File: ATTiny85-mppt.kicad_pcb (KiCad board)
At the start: 2 copper layers, 97.6 x 90.8 mm, 56 parts, among them Q1 BUK9511-55A127, Q2 BUK9511-55A127, Q3 2N2222A, Q4 2N2222A, Q5 2N2904A, U1 LM7805_TO220, U2 LM358N, U3 ATtiny85-20PU

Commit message: refine pcb layout.
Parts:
- moved C6 3.78 mm to (65.7, 66.7), turned to 180 degrees
- moved C3 3.76 mm to (75.8, 44.7), turned to 270 degrees
- moved C5 3.23 mm to (79.6, 66.7), turned to 180 degrees
- moved R9 0.34 mm to (112.5, 54.3)
- moved U3 0.31 mm to (90.4, 49.2)
- moved R12 0.24 mm to (53.0, 56.8)
- moved R16 0.22 mm to (84.9, 56.8)
- moved R8 0.15 mm to (58.2, 56.7)
- moved R15 0.13 mm to (71.5, 76.9)
- moved R10 0.10 mm to (108.1, 54.3)
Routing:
- net GND: track 273.6 -> 300.6 mm
- net /BootStrap: track 73.5 -> 82.2 mm
- net /PV-Current: track 42.6 -> 36.5 mm
- net Net-(Q3-Pad3): track 39.8 -> 34.1 mm
- net Net-(C2-Pad1): track 36.8 -> 32.8 mm
- net Net-(R6-Pad2): track 48.9 -> 52.6 mm
- net /3.6v: track 117.9 -> 114.2 mm
- net Net-(R1-Pad2): track 27.3 -> 28.9 mm
- net Net-(C6-Pad1): track 31.8 -> 33.4 mm
- net Net-(R11-Pad1): track 33.9 -> 35.0 mm

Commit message: rearrange.
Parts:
- C2: value 47uF 50v -> 22uF 50v
- D12: value BZX 55c12(12V) -> Optinal Zenner
- D3: value 1N4001 -> 1N4148
- Q5: value 2N2904A -> 2N2907A
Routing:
- net GND: track 300.6 -> 306.2 mm
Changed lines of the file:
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@@
     (thickness 1.6)
     (drawings 7)
-    (tracks 301)
+    (tracks 303)
     (zones 0)
     (modules 56)
@@
   )
   (setup
-    (last_trace_width 1.5)
+    (last_trace_width 0.25)
     (user_trace_width 0.5)
     (user_trace_width 1)
@@
       (effects (font (size 1 1) (thickness 0.15)))
     )
-    (fp_text value 1N4001 (at 5.08 2.41 180) (layer F.Fab)
+    (fp_text value 1N4148 (at 5.08 2.41 180) (layer F.Fab)
       (effects (font (size 1 1) (thickness 0.15)))
     )
@@
       (effects (font (size 1 1) (thickness 0.15)))
     )
-    (fp_text value "47uF 50v" (at 2.5 7.56) (layer F.Fab)
+    (fp_text value "22uF 50v" (at 2.5 7.56) (layer F.Fab)
       (effects (font (size 1 1) (thickness 0.15)))
     )
@@
       (effects (font (size 1 1) (thickness 0.15)))
     )
-    (fp_text value 2N2904A (at 2.32156 -4.00304 90) (layer F.Fab)
+    (fp_text value 2N2907A (at 2.32156 -4.00304 90) (layer F.Fab)
       (effects (font (size 1 1) (thickness 0.15)))
     )
@@
       (effects (font (size 1 1) (thickness 0.15)))
     )
-    (fp_text value "BZX 55c12(12V)" (at 5.08 2.41) (layer F.Fab)
+    (fp_text value "Optinal Zenner" (at 5.08 2.41) (layer F.Fab)
       (effects (font (size 1 1) (thickness 0.15)))
     )
@@
   (segment (start 75.83932 65.46976) (end 74.58328 66.7258) (width 2) (layer B.Cu) (net 6))
   (segment (start 75.83932 49.7294) (end 75.83932 65.46976) (width 2) (layer B.Cu) (net 6))
+  (segment (start 93.2184 82.1186) (end 90.297 79.1972) (width 1.2) (layer B.Cu) (net 6))
+  (segment (start 93.2184 83.56216) (end 93.2184 82.1186) (width 1.2) (layer B.Cu) (net 6))
   (segment (start 89.22151 54.32552) (end 89.21135 54.33568) (width 1.2) (layer F.Cu) (net 7))
   (segment (start 90.35288 54.32552) (end 89.22151 54.32552) (width 1.2) (layer F.Cu) (net 7))

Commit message: rearrange lines.
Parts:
- D12: footprint Diodes_THT:D_DO-41_SOD81_P10.16mm_Horizontal -> Diodes_THT:D_DO-41_SOD81_P5.08mm_Vertical_AnodeUp
- moved D12 7.39 mm to (119.0, 31.5)
- moved Q2 3.15 mm to (111.6, 29.4)
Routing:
- net PRI_LO: track 94.1 -> 137.1 mm
- net Net-(C7-Pad1): track 84.3 -> 114.6 mm
- net Net-(D1-Pad1): track 85.1 -> 111.5 mm
- net GND: track 306.2 -> 330.0 mm
- net Net-(C2-Pad2): track 50.8 -> 60.0 mm
- net Net-(D12-Pad1): track 11.7 -> 19.2 mm
- net +24V: track 29.3 -> 33.9 mm

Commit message: update
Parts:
- R11: value 100k -> 4.7k
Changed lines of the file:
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@@
   )
   (setup
-    (last_trace_width 1.5)
+    (last_trace_width 0.25)
     (user_trace_width 0.5)
     (user_trace_width 1)
@@
       (effects (font (size 1 1) (thickness 0.15)))
     )
-    (fp_text value 100k (at 7.07644 -2.13868 90) (layer F.Fab)
-      (effects (font (size 1 1) (thickness 0.15)))
-    )
+    (fp_text value 4.7k (at 7.07644 -2.13868 90) (layer F.Fab)
+      (effects (font (size 1 1) (thickness 0.15)))
+    )

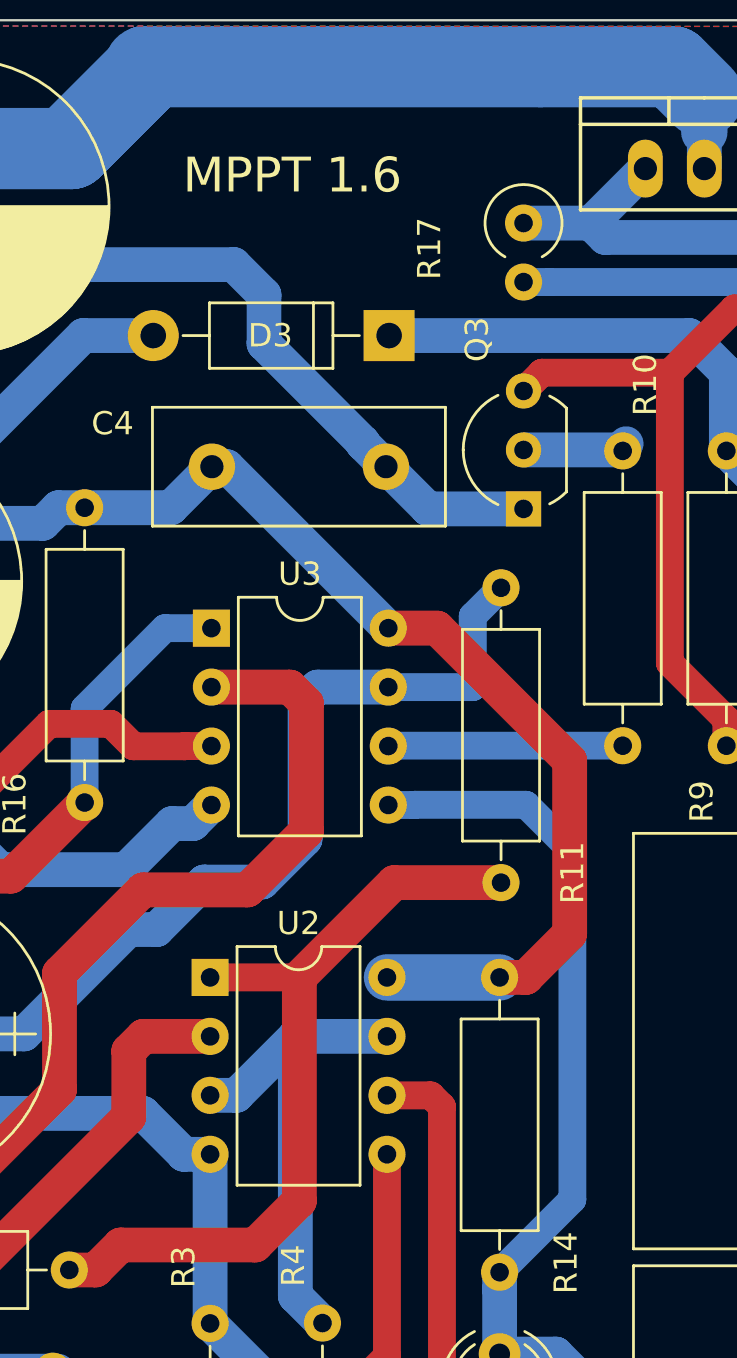
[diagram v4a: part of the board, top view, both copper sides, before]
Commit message: Remove R11 on PCB layout.
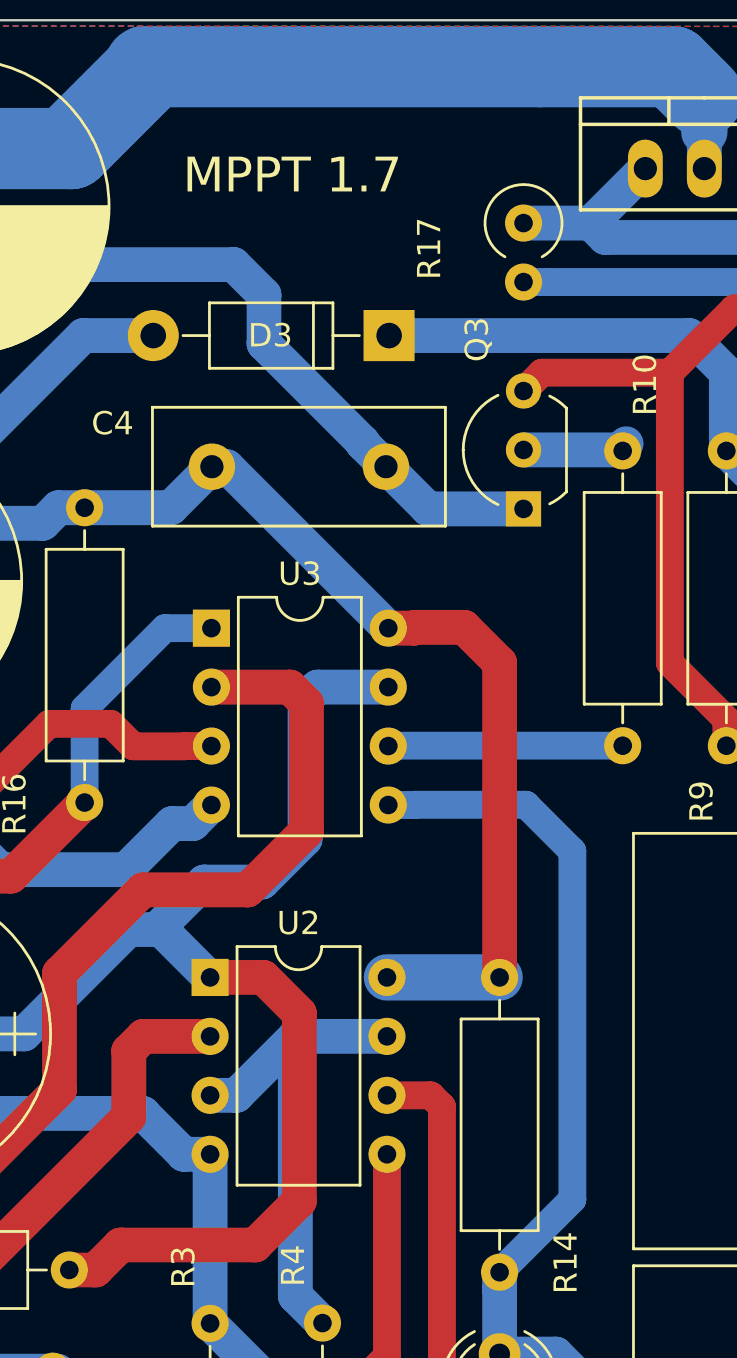
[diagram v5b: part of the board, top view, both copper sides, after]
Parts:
- removed R11: 4.7k, Resistors_THT:R_Axial_DIN0309_L9.0mm_D3.2mm_P12.70mm_Horizontal
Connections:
- R15 pad 2: Net-(R11-Pad1) -> /PV-Current
- U2 pad 1: Net-(R11-Pad1) -> /PV-Current
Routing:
- net Net-(R11-Pad1): track 35.0 -> 0.00 mm
- net /PV-Current: track 36.5 -> 54.9 mm
- net /BootStrap: track 82.2 -> 79.8 mm
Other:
- board text added: "MPPT 1.7"
- board text removed: "MPPT 1.6"

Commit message: update PCB.
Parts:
- removed R17: 1k, Resistors_THT:R_Axial_DIN0309_L9.0mm_D3.2mm_P2.54mm_Vertical
- moved D9 1.18 mm to (103.7, 89.5)
- moved D8 1.09 mm to (103.7, 83.6)
- moved R14 0.92 mm to (103.7, 64.3)
- moved R10 0.16 mm to (107.9, 54.3)
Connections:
- Q4 pad 1: Net-(Q4-Pad1) -> Net-(D12-Pad1)
- Q5 pad 1: Net-(Q4-Pad1) -> Net-(D12-Pad1)
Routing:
- net GND: track 330.0 -> 379.4 mm
- net +24V: track 33.9 -> 73.0 mm
- net Net-(C7-Pad1): track 114.6 -> 136.5 mm
- net Net-(Q4-Pad1): track 21.1 -> 0.00 mm
- net Net-(D1-Pad1): track 111.5 -> 127.1 mm
- net PRI_LO: track 137.1 -> 149.2 mm
- net Net-(C2-Pad2): track 60.0 -> 68.3 mm
- net Net-(D12-Pad1): track 19.2 -> 25.9 mm
- net Net-(Q3-Pad3): track 34.1 -> 39.0 mm
- net /3.6v: track 114.2 -> 109.8 mm
- net /BootStrap: track 79.8 -> 81.5 mm

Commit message: update PCB.
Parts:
- removed C6: 10u, Capacitors_THT:CP_Radial_D12.5mm_P5.00mm
- added Q6: 2N2222A, TO_SOT_Packages_THT:TO-92_Inline_Wide, F.Cu at (58.2, 60.7)
- added Q7: 2N2222A, TO_SOT_Packages_THT:TO-92_Inline_Wide, F.Cu at (63.9, 65.8)
- C2: value 22uF 50v -> 22uF(or 10uF) 50v
- R15: value 10k -> 2.2k
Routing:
- net Net-(R8-Pad2): track 33.4 -> 21.2 mm
- net Net-(Q6-Pad2): track 0.00 -> 10.8 mm
- net GND: track 379.4 -> 373.7 mm
- net /PV-Voltage: track 9.69 -> 13.7 mm
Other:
- board text added: "MPPT 1.9"
- board text removed: "MPPT 1.7"

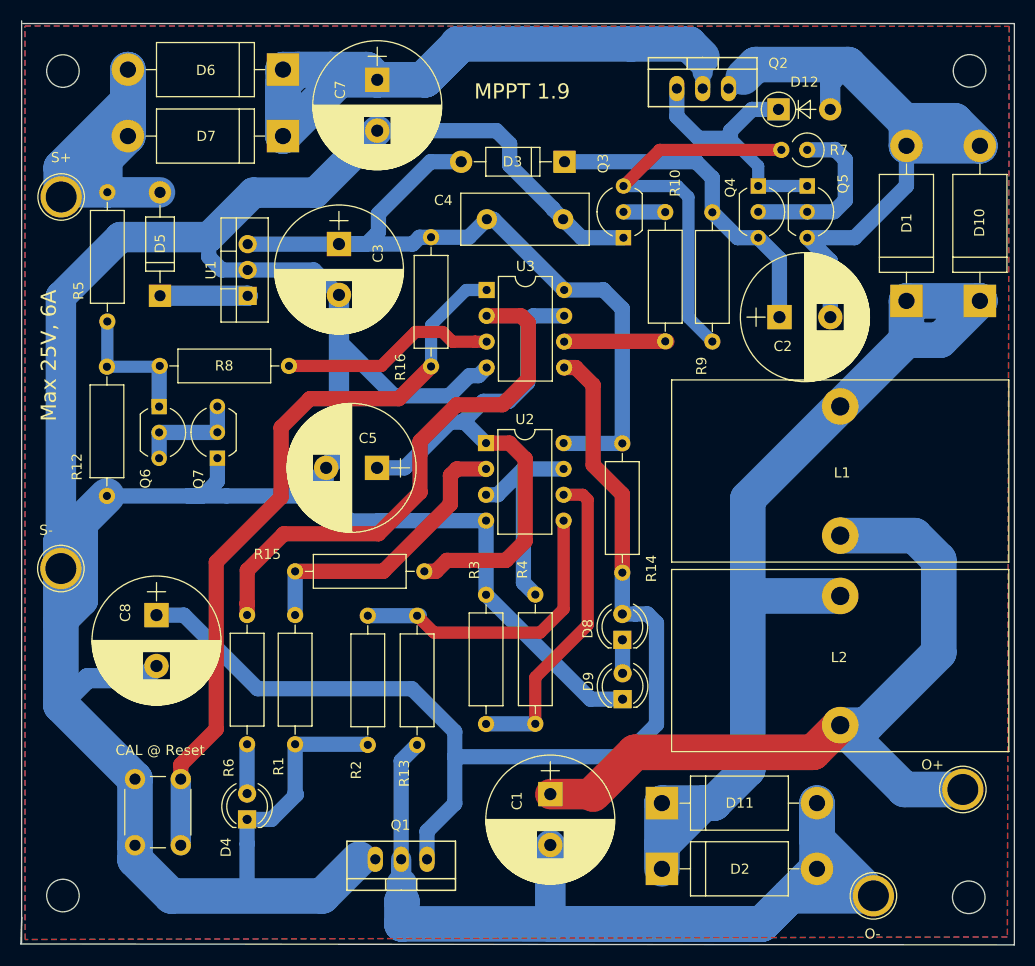
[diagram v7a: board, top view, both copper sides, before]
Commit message: Update circuit. Limit load when control circuit voltage is low.
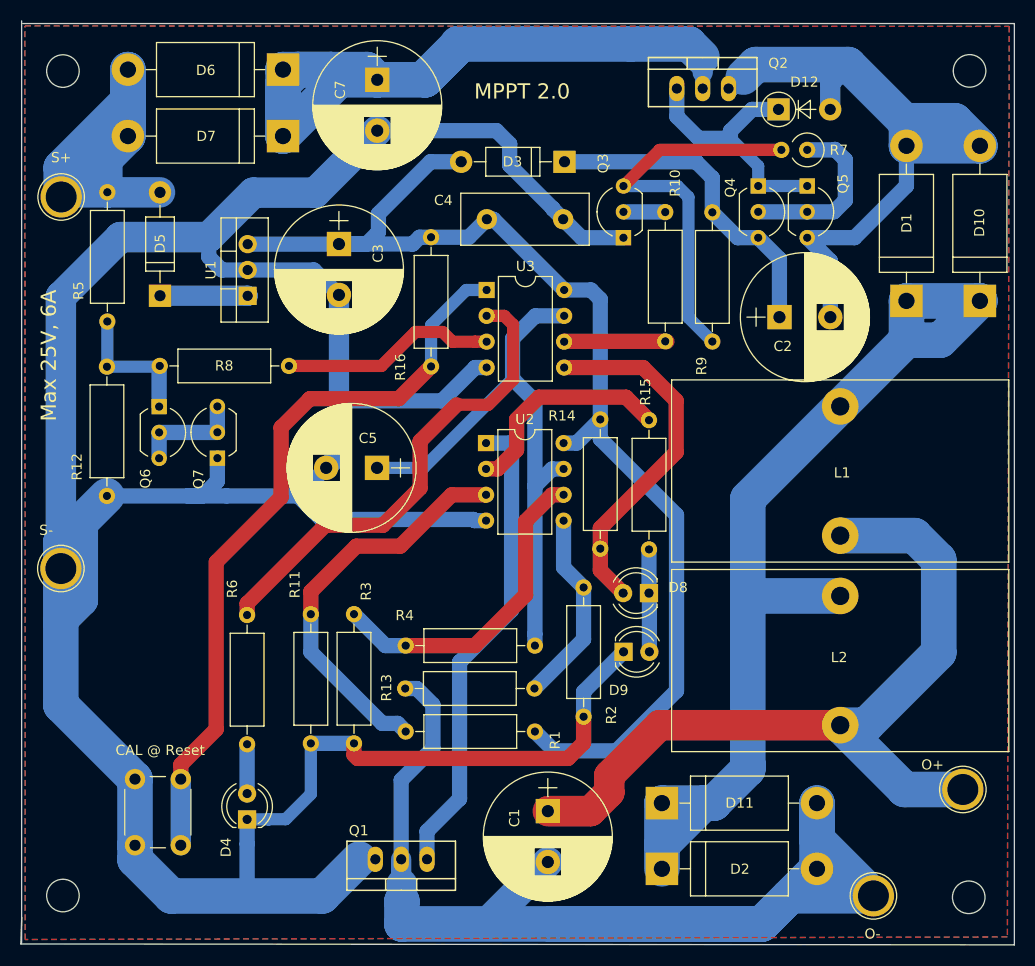
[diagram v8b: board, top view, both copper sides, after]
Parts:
- removed C8: 10u, Capacitors_THT:CP_Radial_D12.5mm_P5.00mm
- added R11: 33k, Resistors_THT:R_Axial_DIN0309_L9.0mm_D3.2mm_P12.70mm_Horizontal, F.Cu at (73.1, 93.8)
- R1: value 2.2k -> 47k
- R15: value 2.2k -> 1k
- R2, R4: value 100k -> 200k
- moved R15 37.8 mm to (106.3, 62.0), turned to 270 degrees
- moved R1 23.6 mm to (95.1, 92.6), turned to 180 degrees
- moved R2 21.4 mm to (99.9, 91.2)
- moved R3 16.9 mm to (77.3, 81.1), turned to 270 degrees
- moved R13 5.66 mm to (82.4, 88.4), turned to 0 degrees
- moved D8 5.29 mm to (106.3, 79.0), turned to 180 degrees
- moved R4 5.01 mm to (95.1, 84.2), turned to 180 degrees
- moved D9 4.65 mm to (103.8, 84.8), turned to 0 degrees
- moved R14 3.20 mm to (101.5, 62.0)
- moved C1 1.69 mm to (96.4, 100.5)
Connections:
- D8 pad 1: Net-(D8-Pad1) -> /1.8v
- D9 pad 2: Net-(D8-Pad1) -> /1.8v
- Q1 pad 1: /3.6v -> Net-(Q1-Pad1)
- R1 pad 1: GND -> /BootStrap
- R1 pad 2: Net-(R1-Pad2) -> /2.06v
- R15 pad 1: Net-(R1-Pad2) -> Net-(R15-Pad1)
- R15 pad 2: /PV-Current -> /1.8v
- R4 pad 1: Net-(R4-Pad1) -> /PV-Current
- U2 pad 1: /PV-Current -> Net-(Q1-Pad1)
- U2 pad 2: Net-(R1-Pad2) -> Net-(R15-Pad1)
- U2 pad 3: Net-(R4-Pad1) -> /2.06v
- U2 pad 7: Net-(R4-Pad1) -> /PV-Current
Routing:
- net /3.6v: track 109.8 -> 35.3 mm
- net Net-(Q1-Pad1): track 0.00 -> 46.7 mm
- net /BootStrap: track 81.5 -> 123.2 mm
- net /2.06v: track 0.00 -> 39.7 mm
- net Net-(R1-Pad2): track 28.9 -> 0.00 mm
- net Net-(R15-Pad1): track 0.00 -> 21.6 mm
- net Net-(R4-Pad1): track 21.5 -> 0.00 mm
- net PRI_LO: track 149.2 -> 166.0 mm
- net Net-(R13-Pad2): track 29.8 -> 19.3 mm
- net /1.8v: track 0.00 -> 10.1 mm
- net Net-(R6-Pad2): track 52.6 -> 47.5 mm
- net GND: track 373.7 -> 369.2 mm
- net /PV-Current: track 54.9 -> 58.7 mm
- net Net-(D8-Pad1): track 3.30 -> 0.00 mm
- net PRI_HI: track 78.4 -> 80.3 mm
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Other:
- board text added: "MPPT 2.0"
- board text removed: "MPPT 1.9"
